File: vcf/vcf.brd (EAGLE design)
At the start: 88.9 x 107.6 mm, 98 parts, among them IC1 OPA4130U, IC2 OPA4130U, IC3 OPA4130U, IC4 OPA4130U, IC5 OPA4130U, Q1 BC847ASMD, Q2 BC847ASMD, Q3 BC847ASMD, Q4 BC847ASMD, Q5 BC847ASMD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

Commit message: made bug fixes.  almost ready to send out again.
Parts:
- removed R21, R27, R28, R43: 1meg, dan:R0603
- C1: value 1n -> 18n
- C2, C3, C4: value 1n -> 36n
- R23: value 100k -> 10k
- R25, R26: value 10k -> 1k
- R44: value 10k -> 100k
- moved R50 74.4 mm to (5.08, 62.2), turned to 270 degrees
- moved R49 69.7 mm to (7.62, 62.2), turned to 90 degrees
- moved R26 37.2 mm to (57.1, 26.7), turned to 90 degrees
- moved R5 28.2 mm to (5.08, 68.6)
- moved C6 26.5 mm to (5.08, 72.4), turned to 90 degrees
- moved R25 23.3 mm to (64.8, 26.7), turned to 90 degrees
- moved R19 22.2 mm to (33.0, 26.7), turned to 90 degrees
- moved R47 6.84 mm to (36.8, 82.5), turned to 270 degrees
- moved R37 5.08 mm to (61.0, 54.6)
- moved R38 5.08 mm to (63.5, 54.6)
- moved R4 3.81 mm to (5.08, 76.2)
- moved R48 3.81 mm to (30.5, 72.4)
- moved R11 3.81 mm to (5.08, 58.4)
- moved R6 3.81 mm to (7.62, 58.4)
- moved R44 2.84 mm to (27.9, 72.4)
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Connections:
- removed net N$43: IC1.12, R43.2, VPEROCT.P$3
- new net N$67: AIN.P$3, GAIN.3
- net GND: no longer R21.1, R27.1, R28.1, R43.1
- net N$18: now also AIN2.P$3, GAIN1.3; no longer AIN.P$3, IC1.3, R21.2
- net N$29: now also R25.1; no longer MODAMT.3
- net N$30: now also R20.1; no longer GAIN1.3
- net N$33: now also MIN.P$3, MODAMT.3; no longer AIN2.P$3, IC1.5, R27.2
- net N$38: now also R26.1; no longer SCALE.E
- net N$40: now also SCALE.E, VPEROCT.P$3; no longer MODAMT.2, R25.1
- net N$41: now also IC1.12; no longer R26.1
- net N$50: now also MODAMT.2; no longer MIN.P$3, R28.2
- net N$57: now also IC1.3; no longer R19.1
- net N$62: now also IC1.5; no longer R20.1
- net N$63: now also R19.1; no longer GAIN.3
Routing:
- net N$57: track 6.12 -> 101.0 mm, vias 0 -> 4
- net N$67: track 0.00 -> 47.7 mm, vias 0 -> 3
- net +12V: track 326.2 -> 371.5 mm, vias 24 -> 28
- net N$29: track 44.7 -> 5.44 mm, vias 1 -> 0
- net N$63: track 69.8 -> 34.0 mm, vias 4 -> 2
- net N$60: track 0.00 -> 31.8 mm, vias 0 -> 2
- net N$50: track 68.5 -> 41.2 mm
- net N$43: track 27.0 -> 0.00 mm, vias 2 -> 0
- net N$62: track 68.9 -> 41.9 mm, vias 6 -> 4
- net N$40: track 6.12 -> 29.5 mm, vias 0 -> 1
- net N$30: track 47.6 -> 69.8 mm
- net N$41: track 39.8 -> 18.2 mm, vias 4 -> 0
- net N$68: track 0.00 -> 20.1 mm
- net N$38: track 24.1 -> 5.44 mm, vias 2 -> 0
- net N$14: track 28.0 -> 46.2 mm, vias 2 -> 4
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
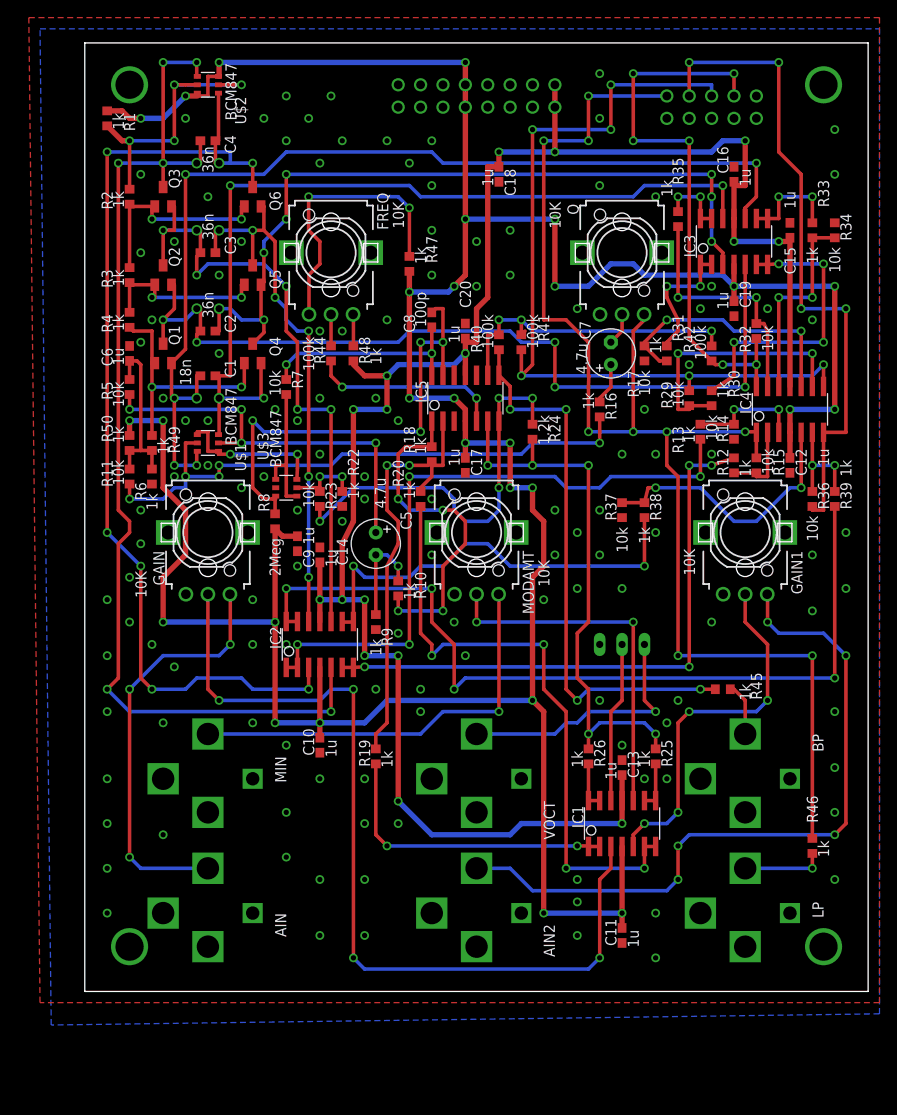
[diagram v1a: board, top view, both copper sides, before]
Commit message: fixed the input impedance situation.
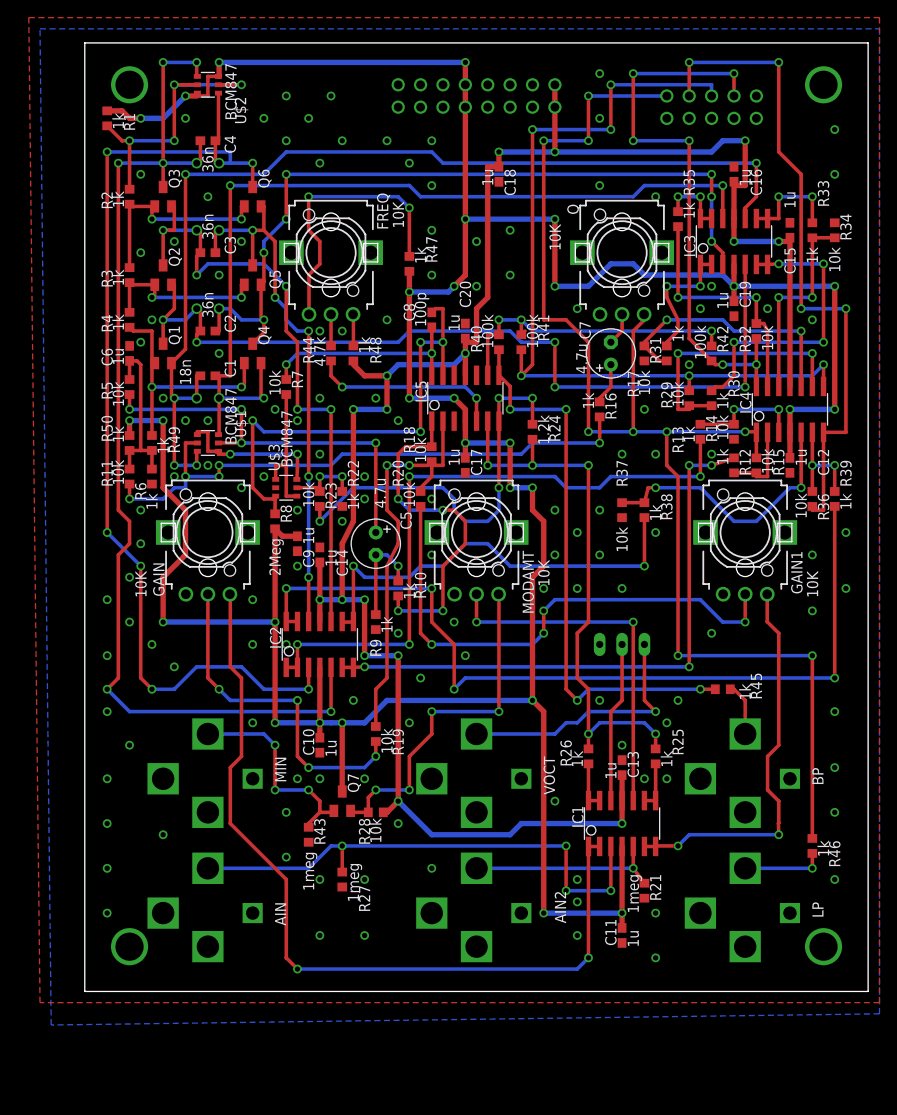
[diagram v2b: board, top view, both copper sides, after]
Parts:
- added Q7: BC847ASMD, dan:SOT23
- added R21, R27, R43: 1meg, dan:R0603
- added R28: 10k, dan:R0603
- R18, R19, R20: value 1k -> 10k
- R44: value 100k -> 4.7k
- SCALE: value 10K -> 100K
- moved R19 2.54 mm to (33.0, 29.2)
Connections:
- removed net N$63: IC1.1, IC1.2, R19.1
- new net N$43: GAIN.2, R19.1
- new net N$69: AIN2.P$3, IC1.5, R21.2
- net +12V: now also Q7.3
- net -12V: now also R28.1
- net GND: now also R21.1, R27.1, R43.1
- net N$18: now also MIN.P$3, Q7.1, R43.2; no longer AIN2.P$3, GAIN1.3
- net N$30: now also GAIN1.3; no longer R20.1
- net N$33: now also Q7.2, R28.2; no longer MIN.P$3
- net N$57: now also GAIN1.2, R20.1; no longer GAIN.2, IC1.3
- net N$62: now also AIN.P$3, IC1.3, R27.2; no longer GAIN1.2, IC1.5
- net N$67: now also IC1.1, IC1.2; no longer AIN.P$3
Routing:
- net N$18: track 81.0 -> 24.0 mm, vias 5 -> 3
- net N$67: track 47.7 -> 94.2 mm, vias 3 -> 2
- net N$57: track 101.0 -> 59.6 mm
- net N$43: track 0.00 -> 39.1 mm, vias 0 -> 4
- net N$63: track 34.0 -> 0.00 mm, vias 2 -> 0
- net N$30: track 69.8 -> 44.7 mm, vias 4 -> 2
- net N$69: track 0.00 -> 22.4 mm, vias 0 -> 1
- net N$62: track 41.9 -> 59.8 mm
- net +12V: track 371.5 -> 379.3 mm, vias 28 -> 29
- net N$33: track 47.4 -> 39.7 mm, vias 1 -> 4
- net N$15: track 49.4 -> 46.8 mm
- net -12V: track 220.6 -> 222.8 mm
- net N$8: track 114.8 -> 115.9 mm

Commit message: moved the tempco to next to the exponentiator pair
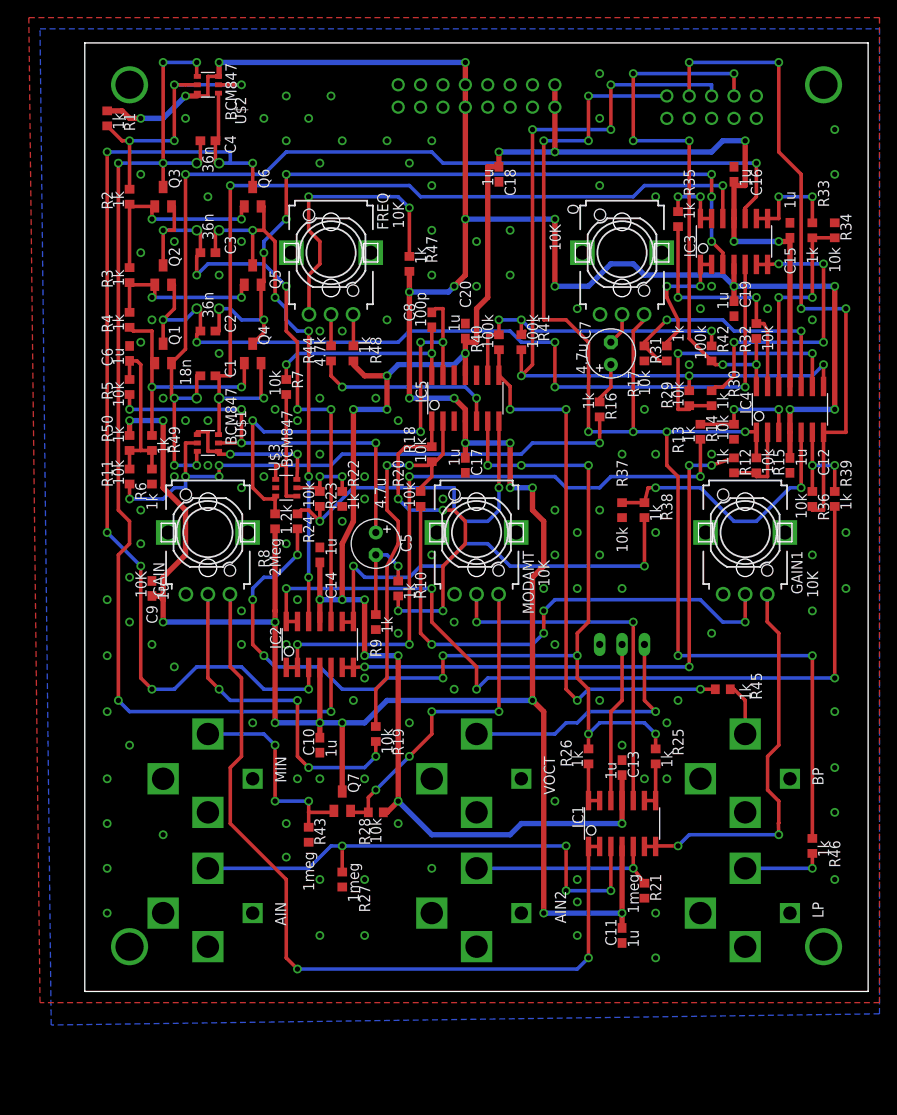
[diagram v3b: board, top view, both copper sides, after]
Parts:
- moved R24 28.5 mm to (24.1, 53.3)
- moved C9 17.3 mm to (7.62, 45.7), turned to 90 degrees
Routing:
- net N$36: track 63.0 -> 118.0 mm, vias 5 -> 11
- net N$53: track 45.9 -> 40.5 mm, vias 4 -> 2
- net N$33: track 39.7 -> 37.4 mm
- net N$42: track 97.2 -> 95.7 mm
- net N$15: track 46.8 -> 45.7 mm
- net N$9: track 124.3 -> 123.2 mm
- net +12V: track 379.3 -> 378.3 mm

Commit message: sent out the vcf board for 2nd revision
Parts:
- moved C16 1.27 mm to (73.7, 94.0)
- moved U$3 1.27 mm to (21.6, 57.1)
- moved R14 1.27 mm to (72.4, 63.5)
- moved R16 1.27 mm to (59.7, 66.0)
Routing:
- net N$2: track 116.9 -> 118.7 mm
- net N$52: track 64.7 -> 66.5 mm
- net N$3: track 98.5 -> 100.3 mm
- net N$34: track 8.95 -> 10.2 mm
- net N$22: track 67.3 -> 68.5 mm
- net N$26: track 13.2 -> 12.3 mm
- net N$61: track 63.4 -> 64.1 mm
- net N$16: track 15.5 -> 14.8 mm
- net N$27: track 153.4 -> 152.7 mm
- net N$1: track 17.1 -> 17.7 mm
- net N$31: track 4.76 -> 4.23 mm

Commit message: fixed values in schematic after getting 2nd board rev back.
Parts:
- R10: value 1k -> 10k
- R25: value 1k -> 2.2k
- R26: value 1k -> 4.7k
- R44: value 4.7k -> 10k
- R47, R48: value 1k -> 100k
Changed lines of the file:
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@@
 <attribute name="VALUE" x="3.175" y="99.695" size="1.27" layer="21" font="vector" ratio="15" rot="R270"/>
 </element>
-<element name="R10" library="dan" package="R0603" value="1k" x="35.56" y="45.72" smashed="yes" rot="R90">
+<element name="R10" library="dan" package="R0603" value="10k" x="35.56" y="45.72" smashed="yes" rot="R90">
 <attribute name="NAME" x="37.465" y="47.625" size="1.27" layer="21" font="vector" ratio="15" rot="R270"/>
 <attribute name="VALUE" x="36.195" y="46.355" size="1.27" layer="21" font="vector" ratio="15" rot="R270"/>
@@
 <attribute name="VALUE" x="22.225" y="55.245" size="1.27" layer="21" font="vector" ratio="15" rot="R270"/>
 </element>
-<element name="R25" library="dan" package="R0603" value="1k" x="64.77" y="26.67" smashed="yes" rot="R90">
+<element name="R25" library="dan" package="R0603" value="2.2k" x="64.77" y="26.67" smashed="yes" rot="R90">
 <attribute name="NAME" x="66.675" y="29.845" size="1.27" layer="21" font="vector" ratio="15" rot="R270"/>
 <attribute name="VALUE" x="65.405" y="27.305" size="1.27" layer="21" font="vector" ratio="15" rot="R270"/>
 </element>
-<element name="R26" library="dan" package="R0603" value="1k" x="57.15" y="26.67" smashed="yes" rot="R90">
+<element name="R26" library="dan" package="R0603" value="4.7k" x="57.15" y="26.67" smashed="yes" rot="R90">
 <attribute name="NAME" x="53.975" y="28.575" size="1.27" layer="21" font="vector" ratio="15" rot="R270"/>
 <attribute name="VALUE" x="55.245" y="27.305" size="1.27" layer="21" font="vector" ratio="15" rot="R270"/>
@@
 <attribute name="VALUE" x="34.95" y="89.59" size="1.27" layer="21" font="vector" ratio="15" rot="R270"/>
 </element>
-<element name="R44" library="dan" package="R0603" value="4.7k" x="27.94" y="72.39" smashed="yes" rot="R270">
+<element name="R44" library="dan" package="R0603" value="10k" x="27.94" y="72.39" smashed="yes" rot="R270">
 <attribute name="NAME" x="24.765" y="74.295" size="1.27" layer="21" font="vector" ratio="15" rot="R270"/>
 <attribute name="VALUE" x="26.035" y="74.295" size="1.27" layer="21" font="vector" ratio="15" rot="R270"/>
@@
 <attribute name="VALUE" x="83.185" y="17.145" size="1.27" layer="21" font="vector" ratio="15" rot="R270"/>
 </element>
-<element name="R47" library="dan" package="R0603" value="1k" x="36.83" y="82.55" smashed="yes" rot="R270">
+<element name="R47" library="dan" package="R0603" value="100k" x="36.83" y="82.55" smashed="yes" rot="R270">
 <attribute name="NAME" x="38.735" y="85.725" size="1.27" layer="21" font="vector" ratio="15" rot="R270"/>
 <attribute name="VALUE" x="37.465" y="84.455" size="1.27" layer="21" font="vector" ratio="15" rot="R270"/>
 </element>
-<element name="R48" library="dan" package="R0603" value="1k" x="30.48" y="72.39" smashed="yes" rot="R90">
+<element name="R48" library="dan" package="R0603" value="100k" x="30.48" y="72.39" smashed="yes" rot="R90">
 <attribute name="NAME" x="32.385" y="74.295" size="1.27" layer="21" font="vector" ratio="15" rot="R270"/>
 <attribute name="VALUE" x="31.115" y="74.295" size="1.27" layer="21" font="vector" ratio="15" rot="R270"/>

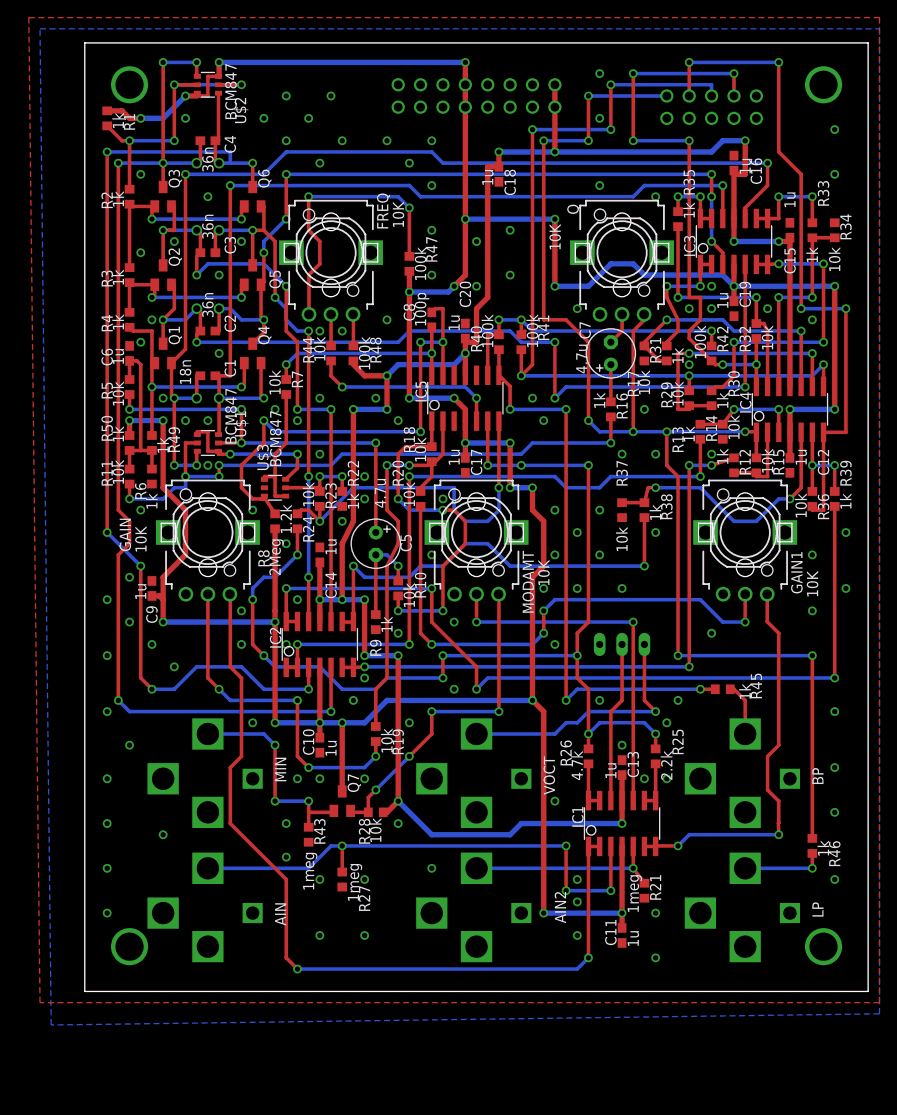
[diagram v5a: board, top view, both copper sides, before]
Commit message: added a vca.  made changes to the filter components
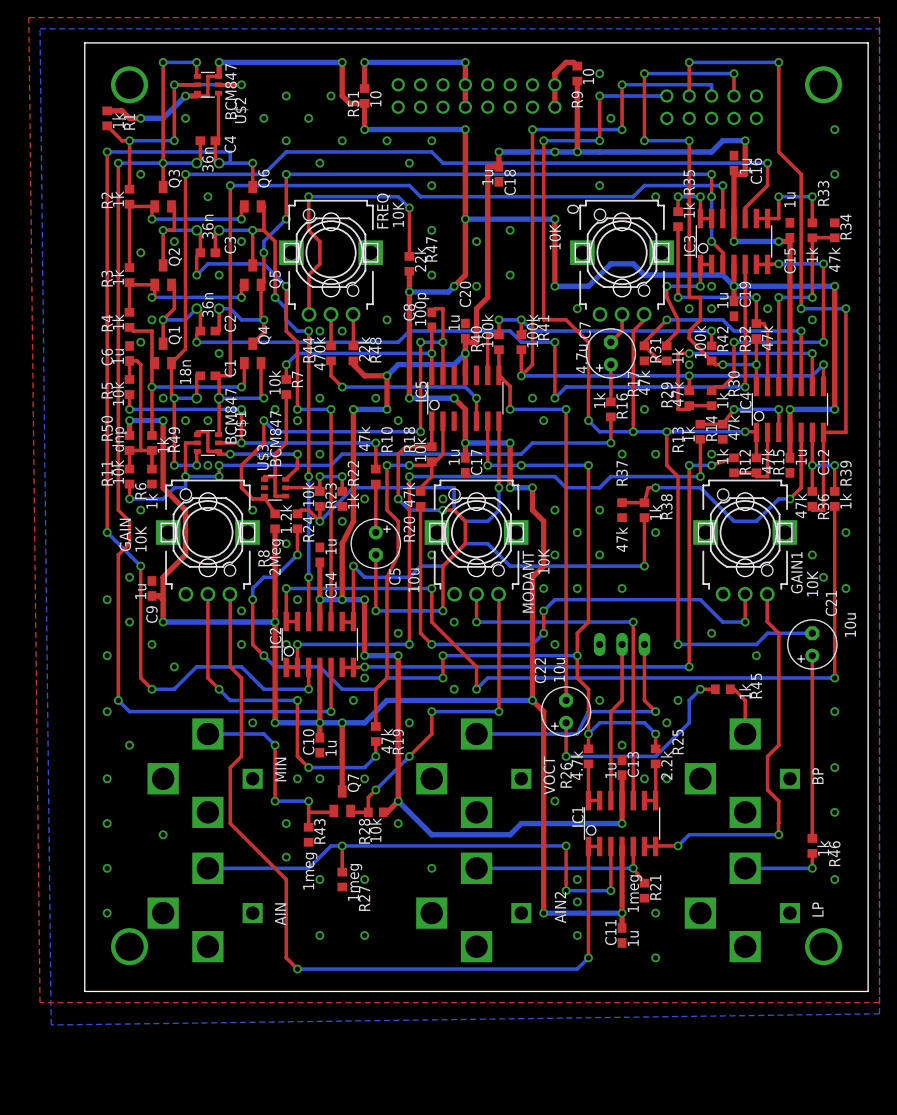
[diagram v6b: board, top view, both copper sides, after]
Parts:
- added C21, C22: 10u, dan:E2,5-6
- added R51: 10, dan:R0603
- C5: value 4.7u -> 10u
- R10, R14, R15, R17, R19, R20, R29, R32, R34, R36, R37: value 10k -> 47k
- R44: value 10k -> 470k
- R47, R48: value 100k -> 22k
- R50: value 1k -> dnp
- R9: value 1k -> 10
- moved R9 66.3 mm to (55.9, 104.1)
- moved R10 13.0 mm to (33.0, 58.4)
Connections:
- new net N$63: C21.+, R46.2
- new net N$70: C22.+, R45.2
- new net N$71: POWER.10, POWER.9, R51.2
- new net N$72: POWER.1, POWER.2, R9.2
- net +12V: now also R51.1; no longer POWER.10, POWER.9
- net -12V: now also R9.1; no longer POWER.1, POWER.2
- net GND: no longer R9.1
- net N$14: now also R10.2; no longer C5.+
- net N$20: now also C5.-; no longer R10.1
- net N$21: now also C5.+, R10.1; no longer C5.-, R10.2, R9.2
- net N$27: now also C21.-; no longer R46.2
- net N$61: now also C22.-; no longer R45.2
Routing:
- net N$70: track 0.00 -> 25.4 mm, vias 0 -> 2
- net N$27: track 152.7 -> 131.2 mm, vias 9 -> 8
- net N$63: track 0.00 -> 20.7 mm
- net N$71: track 0.00 -> 19.5 mm, vias 0 -> 2
- net N$61: track 64.1 -> 46.7 mm, vias 4 -> 2
- net N$20: track 38.8 -> 46.0 mm
- net N$14: track 46.2 -> 39.0 mm
- net N$72: track 0.00 -> 7.05 mm
- net N$21: track 11.5 -> 5.50 mm, vias 1 -> 0
- net N$52: track 66.5 -> 63.9 mm
- net N$40: track 29.5 -> 30.0 mm
- net +12V: track 378.3 -> 377.8 mm, vias 29 -> 31
- net -12V: track 222.8 -> 223.2 mm, vias 16 -> 17
